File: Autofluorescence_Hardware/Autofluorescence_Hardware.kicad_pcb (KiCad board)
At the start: 2 copper layers, 44.4 x 44.5 mm, 26 parts, among them U1 PAM2863ECR, U2 PAM2863ECR, U3 PAM2863ECR

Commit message: Finished layout
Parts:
- added G***: LOGO, tuna:tuna_silkscreen, B.Cu at (149.9, 90.6)
- moved D3 66.5 mm to (169.9, 82.0), turned to -90 degrees
- moved R2 64.5 mm to (169.0, 84.8)
- moved C1 48.8 mm to (145.0, 65.5)
- moved D7 42.0 mm to (142.9, 88.9)
- moved D2 38.3 mm to (153.9, 59.9), turned to 0 degrees
- moved U1 34.8 mm to (149.0, 65.7), turned to 90 degrees
- moved C2 34.2 mm to (161.8, 70.4)
- moved U3 25.2 mm to (146.9, 81.2), turned to -90 degrees
- moved C3 23.2 mm to (151.1, 81.3), turned to -90 degrees
- moved L1 18.7 mm to (155.4, 65.8), turned to 90 degrees
- moved L3 17.8 mm to (155.7, 81.0), turned to -90 degrees
- moved U2 17.7 mm to (161.7, 74.3), turned to 0 degrees
- moved L2 14.0 mm to (163.3, 65.8), turned to 0 degrees
- moved R6 10.4 mm to (136.0, 71.9), turned to 180 degrees
- moved D5 9.57 mm to (164.3, 81.4)
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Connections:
- D1 pad 3: (no net) -> GND
- D4 pad 3: (no net) -> GND
- D6 pad 3: (no net) -> GND
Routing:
- net +12V: track 0.00 -> 54.4 mm, vias 0 -> 4
- net VSET: track 0.00 -> 40.2 mm, vias 0 -> 3
- net Net-(D4-A): track 0.00 -> 26.3 mm, vias 0 -> 4
- net Net-(D7-A): track 0.00 -> 23.8 mm
- net Net-(D5-A): track 0.00 -> 21.2 mm
- net Net-(D1-A): track 0.00 -> 17.0 mm, vias 0 -> 3
- net Net-(D6-A): track 0.00 -> 16.8 mm, vias 0 -> 4
- net Net-(D1-K): track 0.00 -> 12.6 mm, vias 0 -> 3
- net Net-(D4-K): track 0.00 -> 12.1 mm, vias 0 -> 3
- net Net-(D6-K): track 0.00 -> 11.4 mm, vias 0 -> 3
- net Net-(D2-A): track 0.00 -> 10.2 mm
- net Net-(D3-A): track 0.00 -> 1.94 mm
- net GND: vias 27 -> 46
- added copper zone on F.Cu, net +12V
- added copper zone on B.Cu, net Net-(D1-A)
- added copper zone on B.Cu, net Net-(D1-K)
- added copper zone on B.Cu, net Net-(D4-A)
- added copper zone on B.Cu, net Net-(D4-K)
- added copper zone on B.Cu, net Net-(D6-A)
- added copper zone on B.Cu, net Net-(D6-K)
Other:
- outline, holes or cut-outs redrawn
- board text added: "12V"
- board text added: "Autofluorescence Board Rev1 Mars Rover Design Team Missouri S&T, 2025 Jesse Deuel"

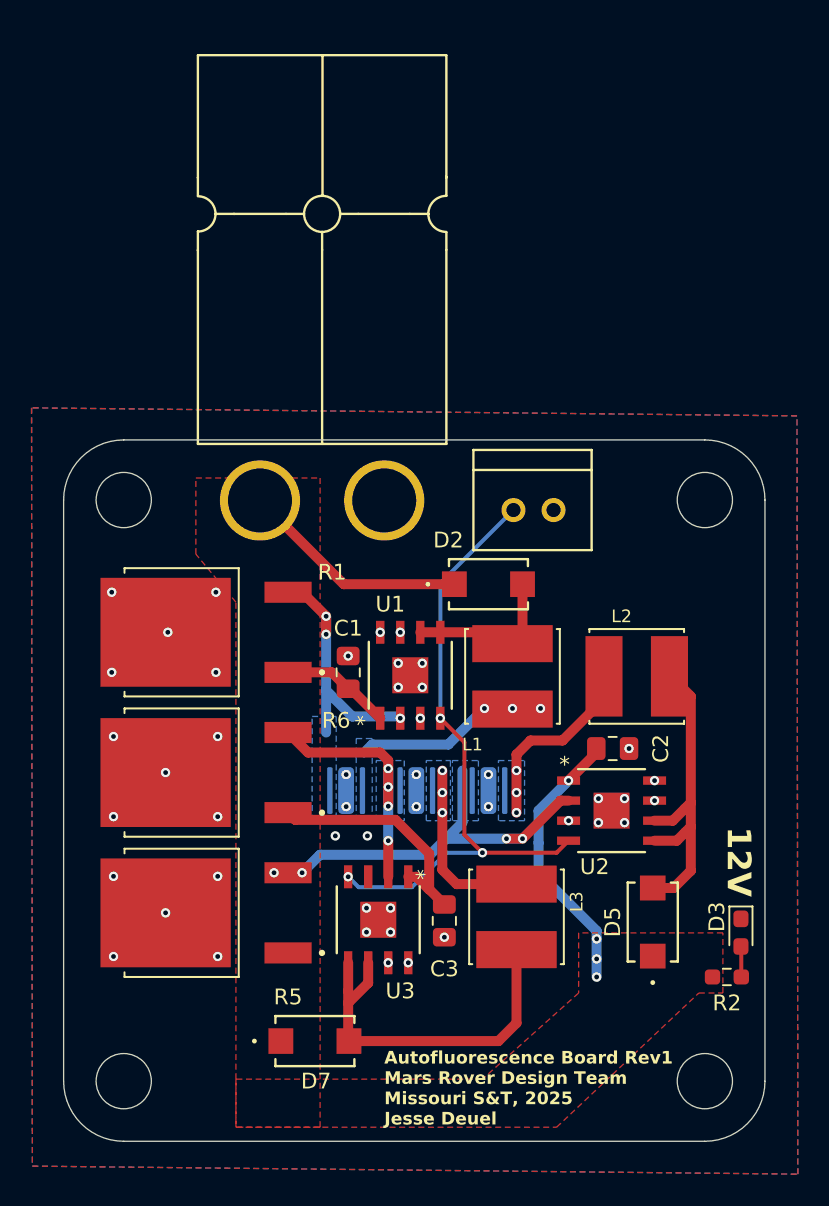
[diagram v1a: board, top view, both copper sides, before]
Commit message: Fixed for aluminum core pcb
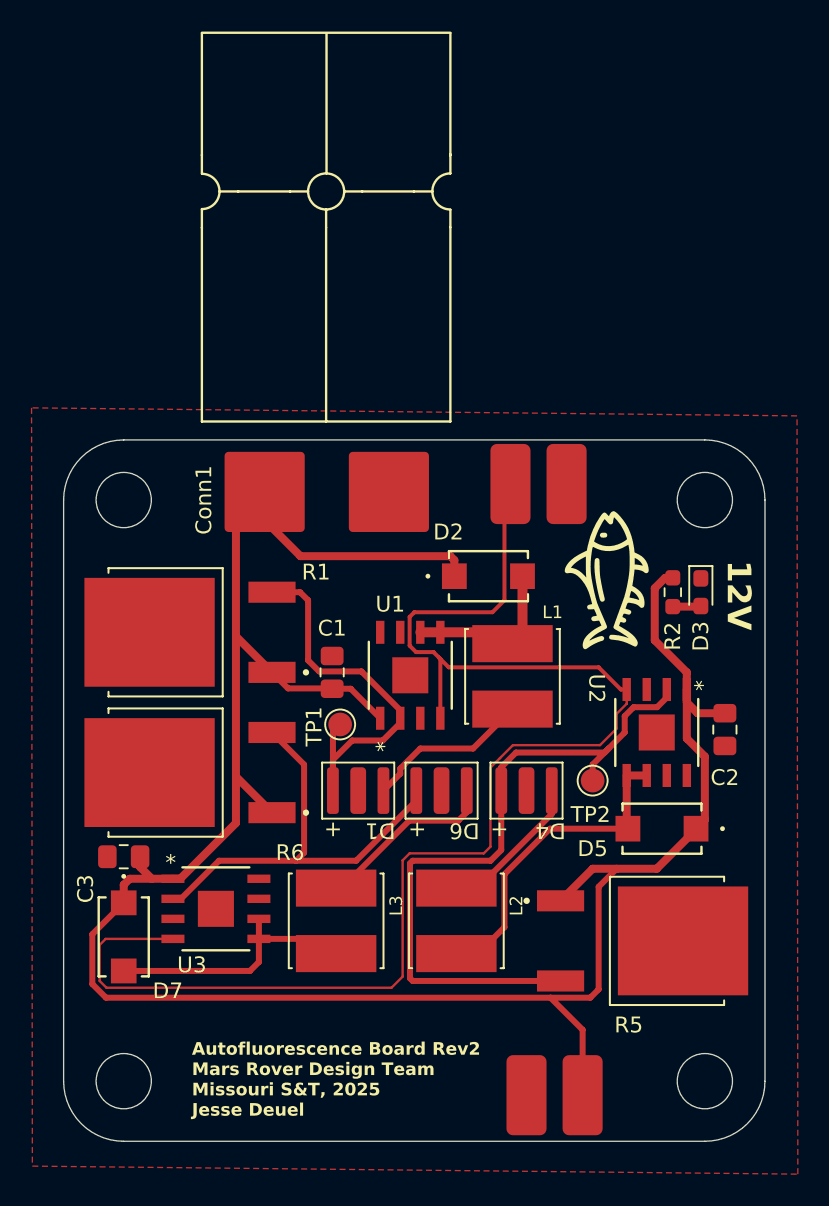
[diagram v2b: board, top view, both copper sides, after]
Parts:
- removed the G*** at (149.9, 90.6)
- added Conn3: Molex_SL_02, MRDT_Connectors:MOLEX_SL_02_Horizontal, F.Cu at (159.4, 94.1)
- added G***: LOGO, KicadLibraries:tuna_silkscreen, F.Cu at (161.4, 59.7)
- added TP1: 380nm, TestPoint:TestPoint_Pad_D1.5mm, F.Cu at (144.5, 68.8)
- added TP2: TestPoint, TestPoint:TestPoint_Pad_D1.5mm, F.Cu at (160.5, 72.4)
- Conn1: footprint MRDT_Connectors:Anderson_2_Horizontal_Side_by_Side -> MRDT_Connectors:Square_Anderson_2_H_Side_By_Side
- Conn2: footprint MRDT_Connectors:MOLEX_SL_02_Vertical -> MRDT_Connectors:MOLEX_SL_02_Horizontal
- D1, D4, D6: moved to F.Cu
- moved R5 27.7 mm to (163.7, 82.5), turned to 0 degrees
- moved R2 24.6 mm to (165.6, 60.5), turned to -90 degrees
- moved D3 21.7 mm to (167.4, 60.5)
- moved C3 20.7 mm to (130.8, 77.2), turned to 180 degrees
- moved L2 19.3 mm to (151.9, 81.3), turned to -90 degrees
- moved D7 13.8 mm to (130.8, 82.3), turned to -90 degrees
- moved L3 11.4 mm to (144.3, 81.3)
- moved U3 10.3 mm to (136.7, 80.5), turned to 0 degrees
- moved C2 7.21 mm to (168.9, 69.2), turned to -90 degrees
- moved D5 5.95 mm to (164.9, 75.4), turned to 180 degrees
- moved U2 5.72 mm to (164.6, 69.3), turned to -90 degrees
- moved Conn2 3.19 mm to (155.8, 52.1)
- moved D4 2.41 mm to (156.3, 73.0)
- moved D6 1.60 mm to (151.0, 73.0)
- moved Conn1 1.30 mm to (148.1, 53.6)
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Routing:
- net +12V: track 54.4 -> 149.7 mm, vias 4 -> 0
- net VSET: track 40.2 -> 91.4 mm, vias 3 -> 0
- net Net-(D4-A): track 26.3 -> 44.2 mm, vias 4 -> 0
- net Net-(D6-A): track 16.8 -> 27.8 mm, vias 4 -> 0
- net Net-(D1-A): track 17.0 -> 26.3 mm, vias 3 -> 0
- net Net-(D7-A): track 23.8 -> 16.8 mm
- net Net-(D4-K): track 12.1 -> 9.47 mm, vias 3 -> 0
- net Net-(D1-K): track 12.6 -> 10.5 mm, vias 3 -> 0
- net Net-(D5-A): track 21.2 -> 22.2 mm
- net Net-(D2-A): track 10.2 -> 10.7 mm
- net Net-(D6-K): track 11.4 -> 11.6 mm, vias 3 -> 0
- net GND: vias 46 -> 0
- removed copper zone on F.Cu, net +12V
- removed copper zone on B.Cu, net GND
- removed copper zone on B.Cu, net Net-(D1-A)
- removed copper zone on B.Cu, net Net-(D1-K)
- removed copper zone on B.Cu, net Net-(D4-A)
- removed copper zone on B.Cu, net Net-(D4-K)
- removed copper zone on B.Cu, net Net-(D6-A)
- removed copper zone on B.Cu, net Net-(D6-K)
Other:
- board text added: "Autofluorescence Board Rev2 Mars Rover Design Team Missouri S&T, 2025 Jesse Deuel"
- board text removed: "Autofluorescence Board Rev1 Mars Rover Design Team Missouri S&T, 2025 Jesse Deuel"
